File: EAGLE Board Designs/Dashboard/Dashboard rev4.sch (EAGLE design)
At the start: 94 parts, among them J1 CONNECTOR-AVR-ISP_2X05_SMD, J2 CONNECTOR-6_μF_S_RA_, J3 CONNECTOR-CAN_μF_S_RA_, J4 CONNECTOR-8_μF_S_RA_, J5 JUMPER_0603_, Q1 TRANSISTOR_N_MOS__PMV15ENEA, Q2 TRANSISTOR_N_MOS__PMV15ENEA, Q3 TRANSISTOR_N_MOS__PMV15ENEA, Q4 TRANSISTOR_N_MOS__PMV15ENEA, Q5 TRANSISTOR_N_MOS__PMV15ENEA, Q6 TRANSISTOR_N_MOS__PMV15ENEA, U1 ATMEGA328P-AU, U2 RE46C100, U3 MCP23S08, U4 MCP2562FD, U5 MCP2515, X1 CRYSTAL_16MHZ, X2 CRYSTAL_16MHZ

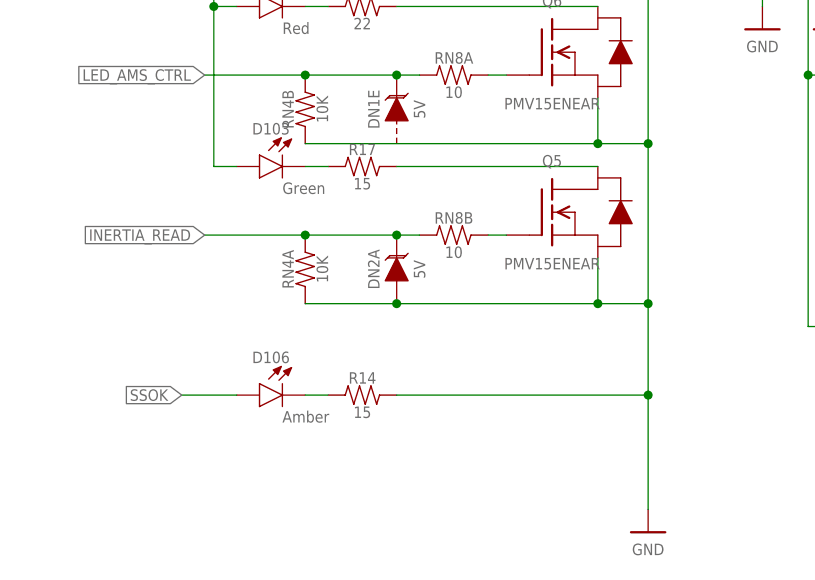
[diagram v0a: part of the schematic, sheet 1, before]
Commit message: SSOK and Inertia Read signals connected to LED nMos switches
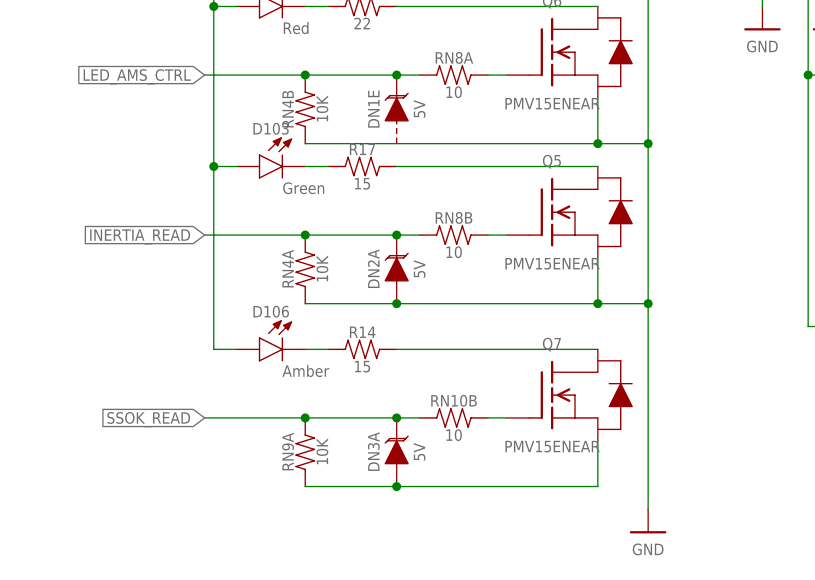
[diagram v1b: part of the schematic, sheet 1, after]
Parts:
- added DN3: TVS_ARRAY_5V, HyTechDevices:TVS_ARRAY_5V
- added Q7: TRANSISTOR_N_MOS__PMV15ENEA, HyTechDevices:TRANSISTOR_N_MOS__PMV15ENEA
- added RN10: RESISTOR_NETWORK_4_10, HyTechDevices:RESISTOR_NETWORK_4_10
- added RN9: RESISTOR_NETWORK_4_10K, HyTechDevices:RESISTOR_NETWORK_4_10K
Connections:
- new net GND1: DN3A.A, Q7.S, RN9A.1
- new net N$26: Q7.G, RN10B.2
- new net N$55: Q7.D, R14.2
- net +5V: now also D106.A
- net GND: no longer R14.2
- net SSOK: no longer D106.A
- net SSOK_READ: now also DN3A.C, RN10B.1, RN9A.2
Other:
- moved on the sheet: D106, R14
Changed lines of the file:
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@@
 <attribute name="SIGNAL" value="SSOK"/>
 </part>
+<part name="RN9" library="HyTechDevices" deviceset="RESISTOR_NETWORK_4_*" device="" technology="10K"/>
+<part name="Q7" library="HyTechDevices" deviceset="TRANSISTOR_N_MOS_?_*" device="" technology="PMV15ENEA"/>
+<part name="RN10" library="HyTechDevices" deviceset="RESISTOR_NETWORK_4_*" device="" technology="10"/>
+<part name="DN3" library="HyTechDevices" deviceset="TVS_ARRAY_*" device="" technology="5V"/>
 </parts>
 <sheets>
@@
 <attribute name="NAME" x="31.75" y="69.596" size="1.27" layer="96" align="bottom-center"/>
 </instance>
-<instance part="D106" gate="LED" x="33.02" y="22.86" smashed="yes">
-<attribute name="COLOR" x="33.02" y="21.082" size="1.27" layer="95" align="top-left"/>
-<attribute name="NAME" x="31.75" y="26.416" size="1.27" layer="96" align="bottom-center"/>
+<instance part="D106" gate="LED" x="33.02" y="27.94" smashed="yes">
+<attribute name="COLOR" x="33.02" y="26.162" size="1.27" layer="95" align="top-left"/>
+<attribute name="NAME" x="31.75" y="31.496" size="1.27" layer="96" align="bottom-center"/>
 </instance>
 <instance part="D4" gate="G$1" x="30.48" y="170.18" smashed="yes">
@@
 <attribute name="RESISTANCE" x="41.91" y="64.77" size="1.27" layer="96" align="top-center"/>
 </instance>
-<instance part="R14" gate="G$1" x="43.18" y="22.86" smashed="yes">
-<attribute name="NAME" x="41.91" y="24.13" size="1.27" layer="95" align="bottom-center"/>
-<attribute name="RESISTANCE" x="41.91" y="21.59" size="1.27" layer="96" align="top-center"/>
+<instance part="R14" gate="G$1" x="43.18" y="27.94" smashed="yes">
+<attribute name="NAME" x="41.91" y="29.21" size="1.27" layer="95" align="bottom-center"/>
+<attribute name="RESISTANCE" x="41.91" y="26.67" size="1.27" layer="96" align="top-center"/>
 </instance>
 <instance part="R8" gate="G$1" x="43.18" y="137.16" smashed="yes">
@@
 <attribute name="MPN" x="99.06" y="92.202" size="1.27" layer="95" rot="MR0" align="top-left"/>
 <attribute name="SIGNAL" x="96.52" y="93.98" size="1.778" layer="96" display="off"/>
+</instance>
+<instance part="RN9" gate="A" x="35.56" y="17.78" smashed="yes" rot="R90">
+<attribute name="NAME" x="34.29" y="16.51" size="1.27" layer="95" rot="R90" align="bottom-center"/>
+<attribute name="RESISTANCE" x="36.83" y="16.51" size="1.27" layer="96" rot="R90" align="top-center"/>
+</instance>
+<instance part="Q7" gate="G$1" x="62.992" y="22.86" smashed="yes">
+<attribute name="NAME" x="62.992" y="27.94" size="1.27" layer="95" align="bottom-center"/>
+<attribute name="MPN" x="62.992" y="17.78" size="1.27" layer="95" align="top-center"/>
+</instance>
+<instance part="RN10" gate="B" x="53.34" y="20.32" smashed="yes">
+<attribute name="NAME" x="52.07" y="21.59" size="1.27" layer="95" align="bottom-center"/>
+<attribute name="RESISTANCE" x="52.07" y="19.05" size="1.27" layer="96" align="top-center"/>
+</instance>
+<instance part="DN3" gate="A" x="45.72" y="17.78" smashed="yes" rot="R90">
+<attribute name="NAME" x="43.815" y="16.51" size="1.27" layer="95" rot="R90" align="bottom-center"/>
+<attribute name="VOLTAGE" x="47.625" y="16.51" size="1.27" layer="96" rot="R90" align="top-center"/>
 </instance>
 </instances>
@@
 </segment>
 <segment>
-<wire x1="45.72" y1="22.86" x2="73.66" y2="22.86" width="0.1524" layer="91"/>
-<wire x1="73.66" y1="10.16" x2="73.66" y2="22.86" width="0.1524" layer="91"/>
-<junction x="73.66" y="22.86"/>
-<wire x1="73.66" y1="22.86" x2="73.66" y2="33.02" width="0.1524" layer="91"/>
+<wire x1="73.66" y1="10.16" x2="73.66" y2="33.02" width="0.1524" layer="91"/>
 <wire x1="73.66" y1="33.02" x2="73.66" y2="50.8" width="0.1524" layer="91"/>
 <wire x1="73.66" y1="50.8" x2="73.66" y2="68.58" width="0.1524" layer="91"/>
@@
 <pinref part="RN6" gate="C" pin="1"/>
 <junction x="73.66" y="142.24"/>
-<pinref part="R14" gate="G$1" pin="2"/>
 </segment>
 <segment>
@@
 <junction x="25.4" y="144.78"/>
 <pinref part="P35" gate="1" pin="+5V"/>
+<wire x1="25.4" y1="48.26" x2="25.4" y2="27.94" width="0.1524" layer="91"/>
+<junction x="25.4" y="48.26"/>
+<pinref part="D106" gate="LED" pin="A"/>
+<wire x1="25.4" y1="27.94" x2="27.94" y2="27.94" width="0.1524" layer="91"/>
 </segment>
 <segment>
@@
 <net name="SSOK" class="0">
 <segment>
-<label x="21.844" y="22.86" size="1.27" layer="95" rot="R180" xref="yes"/>
-<pinref part="D106" gate="LED" pin="A"/>
-<wire x1="27.94" y1="22.86" x2="21.844" y2="22.86" width="0.1524" layer="91"/>
-</segment>
-<segment>
 <wire x1="99.06" y1="88.9" x2="93.98" y2="88.9" width="0.1524" layer="91"/>
 <label x="91.44" y="88.9" size="1.27" layer="95" rot="R180" xref="yes"/>
@@
 <pinref part="U1" gate="G$1" pin="A6"/>
 </segment>
+<segment>
+<label x="24.384" y="20.32" size="1.27" layer="95" rot="R180" xref="yes"/>
+<pinref part="RN9" gate="A" pin="2"/>
+<wire x1="24.384" y1="20.32" x2="35.56" y2="20.32" width="0.1524" layer="91"/>
+<wire x1="35.56" y1="20.32" x2="45.72" y2="20.32" width="0.1524" layer="91"/>
+<junction x="35.56" y="20.32"/>
+<pinref part="RN10" gate="B" pin="1"/>
+<pinref part="DN3" gate="A" pin="C"/>
+<wire x1="45.72" y1="20.32" x2="48.26" y2="20.32" width="0.1524" layer="91"/>
+<junction x="45.72" y="20.32"/>
+</segment>
 </net>
 <net name="SHUTDOWN_H" class="0">
@@
 <pinref part="D100" gate="LED" pin="C"/>
 <pinref part="R16" gate="G$1" pin="1"/>
-</segment>
-</net>
-<net name="N$26" class="0">
-<segment>
-<wire x1="38.1" y1="22.86" x2="35.56" y2="22.86" width="0.1524" layer="91"/>
-<pinref part="D106" gate="LED" pin="C"/>
-<pinref part="R14" gate="G$1" pin="1"/>
 </segment>
 </net>
@@
 </segment>
 </net>
+<net name="GND1" class="0">
+<segment>
+<wire x1="35.56" y1="12.7" x2="45.72" y2="12.7" width="0.1524" layer="91"/>
+<wire x1="45.72" y1="12.7" x2="68.072" y2="12.7" width="0.1524" layer="91"/>
+<pinref part="Q7" gate="G$1" pin="S"/>
+<wire x1="68.072" y1="17.78" x2="68.072" y2="12.7" width="0.1524" layer="91"/>
+<pinref part="RN9" gate="A" pin="1"/>
+<junction x="45.72" y="12.7"/>
+<pinref part="DN3" gate="A" pin="A"/>
+</segment>
+</net>
+<net name="N$26" class="0">
+<segment>
+<pinref part="RN10" gate="B" pin="2"/>
+<pinref part="Q7" gate="G$1" pin="G"/>
+<wire x1="55.88" y1="20.32" x2="57.912" y2="20.32" width="0.1524" layer="91"/>
+</segment>
+</net>
+<net name="N$49" class="0">
+<segment>
+<pinref part="D106" gate="LED" pin="C"/>
+<pinref part="R14" gate="G$1" pin="1"/>
+<wire x1="35.56" y1="27.94" x2="38.1" y2="27.94" width="0.1524" layer="91"/>
+</segment>
+</net>
+<net name="N$55" class="0">
+<segment>
+<pinref part="R14" gate="G$1" pin="2"/>
+<pinref part="Q7" gate="G$1" pin="D"/>
+<wire x1="45.72" y1="27.94" x2="68.072" y2="27.94" width="0.1524" layer="91"/>
+</segment>
+</net>

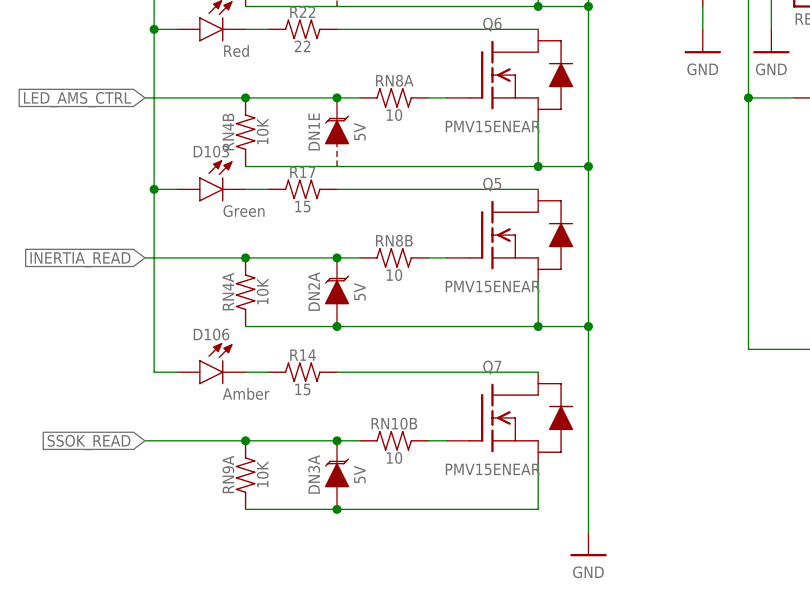
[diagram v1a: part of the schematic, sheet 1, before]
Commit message: Added inertia and ssok led circuitry, flipped LED, and rerouted
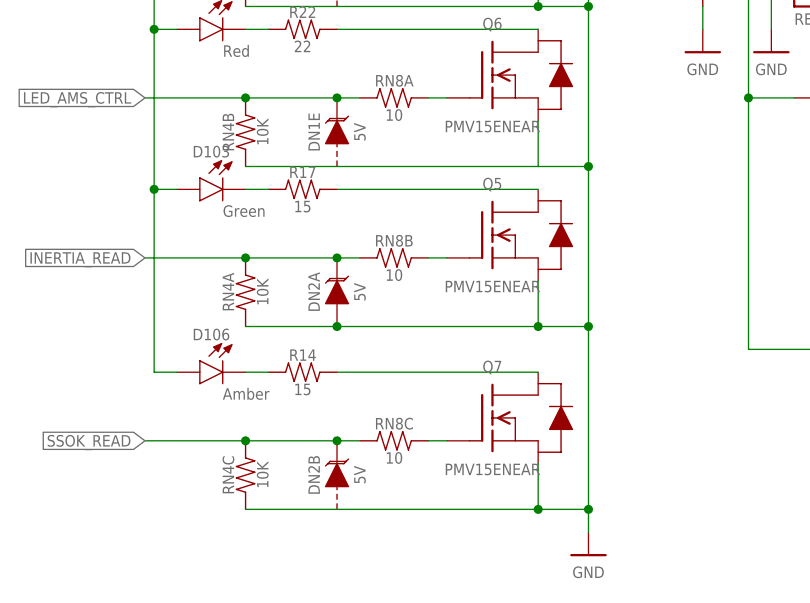
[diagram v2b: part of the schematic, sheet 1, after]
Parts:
- removed DN3: TVS_ARRAY_5V, HyTechDevices:TVS_ARRAY_5V
- removed RN10: RESISTOR_NETWORK_4_10, HyTechDevices:RESISTOR_NETWORK_4_10
- removed RN9: RESISTOR_NETWORK_4_10K, HyTechDevices:RESISTOR_NETWORK_4_10K
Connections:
- removed net GND1: DN3A.A, Q7.S, RN9A.1
- net GND: now also Q7.S, RN4C.1
- net N$26: now also RN8C.2; no longer RN10B.2
- net SSOK_READ: now also DN2B.C, RN4C.2, RN8C.1; no longer DN3A.C, RN10B.1, RN9A.2
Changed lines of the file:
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@@
 <attribute name="SIGNAL" value="SSOK"/>
 </part>
-<part name="RN9" library="HyTechDevices" deviceset="RESISTOR_NETWORK_4_*" device="" technology="10K"/>
 <part name="Q7" library="HyTechDevices" deviceset="TRANSISTOR_N_MOS_?_*" device="" technology="PMV15ENEA"/>
-<part name="RN10" library="HyTechDevices" deviceset="RESISTOR_NETWORK_4_*" device="" technology="10"/>
-<part name="DN3" library="HyTechDevices" deviceset="TVS_ARRAY_*" device="" technology="5V"/>
 </parts>
 <sheets>
@@
 <attribute name="SIGNAL" x="96.52" y="93.98" size="1.778" layer="96" display="off"/>
 </instance>
-<instance part="RN9" gate="A" x="35.56" y="17.78" smashed="yes" rot="R90">
-<attribute name="NAME" x="34.29" y="16.51" size="1.27" layer="95" rot="R90" align="bottom-center"/>
-<attribute name="RESISTANCE" x="36.83" y="16.51" size="1.27" layer="96" rot="R90" align="top-center"/>
-</instance>
 <instance part="Q7" gate="G$1" x="62.992" y="22.86" smashed="yes">
 <attribute name="NAME" x="62.992" y="27.94" size="1.27" layer="95" align="bottom-center"/>
 <attribute name="MPN" x="62.992" y="17.78" size="1.27" layer="95" align="top-center"/>
 </instance>
-<instance part="RN10" gate="B" x="53.34" y="20.32" smashed="yes">
+<instance part="RN8" gate="C" x="53.34" y="20.32" smashed="yes">
 <attribute name="NAME" x="52.07" y="21.59" size="1.27" layer="95" align="bottom-center"/>
 <attribute name="RESISTANCE" x="52.07" y="19.05" size="1.27" layer="96" align="top-center"/>
 </instance>
-<instance part="DN3" gate="A" x="45.72" y="17.78" smashed="yes" rot="R90">
+<instance part="RN4" gate="C" x="35.56" y="17.78" smashed="yes" rot="R90">
+<attribute name="NAME" x="34.29" y="16.51" size="1.27" layer="95" rot="R90" align="bottom-center"/>
+<attribute name="RESISTANCE" x="36.83" y="16.51" size="1.27" layer="96" rot="R90" align="top-center"/>
+</instance>
+<instance part="DN2" gate="B" x="45.72" y="17.78" smashed="yes" rot="R90">
 <attribute name="NAME" x="43.815" y="16.51" size="1.27" layer="95" rot="R90" align="bottom-center"/>
 <attribute name="VOLTAGE" x="47.625" y="16.51" size="1.27" layer="96" rot="R90" align="top-center"/>
@@
 </segment>
 <segment>
-<wire x1="73.66" y1="10.16" x2="73.66" y2="33.02" width="0.1524" layer="91"/>
+<wire x1="73.66" y1="10.16" x2="73.66" y2="12.7" width="0.1524" layer="91"/>
+<wire x1="73.66" y1="12.7" x2="73.66" y2="33.02" width="0.1524" layer="91"/>
 <wire x1="73.66" y1="33.02" x2="73.66" y2="50.8" width="0.1524" layer="91"/>
 <wire x1="73.66" y1="50.8" x2="73.66" y2="68.58" width="0.1524" layer="91"/>
@@
 <wire x1="68.072" y1="68.58" x2="73.66" y2="68.58" width="0.1524" layer="91"/>
 <junction x="73.66" y="50.8"/>
-<wire x1="35.56" y1="50.8" x2="68.072" y2="50.8" width="0.1524" layer="91"/>
-<wire x1="68.072" y1="50.8" x2="73.66" y2="50.8" width="0.1524" layer="91"/>
 <junction x="73.66" y="33.02"/>
 <pinref part="Q1" gate="G$1" pin="S"/>
+<wire x1="68.072" y1="50.8" x2="73.66" y2="50.8" width="0.1524" layer="91"/>
 <wire x1="35.56" y1="33.02" x2="45.72" y2="33.02" width="0.1524" layer="91"/>
 <wire x1="45.72" y1="33.02" x2="68.072" y2="33.02" width="0.1524" layer="91"/>
@@
 <pinref part="Q6" gate="G$1" pin="S"/>
 <wire x1="68.072" y1="55.88" x2="68.072" y2="50.8" width="0.1524" layer="91"/>
-<junction x="68.072" y="50.8"/>
 <pinref part="Q5" gate="G$1" pin="S"/>
 <wire x1="68.072" y1="38.1" x2="68.072" y2="33.02" width="0.1524" layer="91"/>
@@
 <pinref part="RN1" gate="C" pin="1"/>
 <pinref part="RN1" gate="A" pin="1"/>
-<pinref part="RN4" gate="B" pin="1"/>
 <pinref part="RN4" gate="A" pin="1"/>
 <junction x="45.72" y="33.02"/>
@@
 <pinref part="RN6" gate="C" pin="1"/>
 <junction x="73.66" y="142.24"/>
+<pinref part="RN4" gate="B" pin="1"/>
+<wire x1="35.56" y1="50.8" x2="68.072" y2="50.8" width="0.1524" layer="91"/>
+<wire x1="68.072" y1="12.7" x2="73.66" y2="12.7" width="0.1524" layer="91"/>
+<junction x="73.66" y="12.7"/>
+<pinref part="Q7" gate="G$1" pin="S"/>
+<wire x1="68.072" y1="17.78" x2="68.072" y2="12.7" width="0.1524" layer="91"/>
+<pinref part="RN4" gate="C" pin="1"/>
+<wire x1="68.072" y1="12.7" x2="35.56" y2="12.7" width="0.1524" layer="91"/>
+<junction x="68.072" y="12.7"/>
 </segment>
 <segment>
@@
 <segment>
 <label x="24.384" y="20.32" size="1.27" layer="95" rot="R180" xref="yes"/>
-<pinref part="RN9" gate="A" pin="2"/>
 <wire x1="24.384" y1="20.32" x2="35.56" y2="20.32" width="0.1524" layer="91"/>
+<pinref part="RN8" gate="C" pin="1"/>
+<pinref part="RN4" gate="C" pin="2"/>
 <wire x1="35.56" y1="20.32" x2="45.72" y2="20.32" width="0.1524" layer="91"/>
 <junction x="35.56" y="20.32"/>
-<pinref part="RN10" gate="B" pin="1"/>
-<pinref part="DN3" gate="A" pin="C"/>
+<pinref part="DN2" gate="B" pin="C"/>
 <wire x1="45.72" y1="20.32" x2="48.26" y2="20.32" width="0.1524" layer="91"/>
 <junction x="45.72" y="20.32"/>
@@
 </segment>
 </net>
-<net name="GND1" class="0">
-<segment>
-<wire x1="35.56" y1="12.7" x2="45.72" y2="12.7" width="0.1524" layer="91"/>
-<wire x1="45.72" y1="12.7" x2="68.072" y2="12.7" width="0.1524" layer="91"/>
-<pinref part="Q7" gate="G$1" pin="S"/>
-<wire x1="68.072" y1="17.78" x2="68.072" y2="12.7" width="0.1524" layer="91"/>
-<pinref part="RN9" gate="A" pin="1"/>
-<junction x="45.72" y="12.7"/>
-<pinref part="DN3" gate="A" pin="A"/>
-</segment>
-</net>
 <net name="N$26" class="0">
 <segment>
-<pinref part="RN10" gate="B" pin="2"/>
 <pinref part="Q7" gate="G$1" pin="G"/>
 <wire x1="55.88" y1="20.32" x2="57.912" y2="20.32" width="0.1524" layer="91"/>
-</segment>
-</net>
+<pinref part="RN8" gate="C" pin="2"/>
+</segment>
+</net>
